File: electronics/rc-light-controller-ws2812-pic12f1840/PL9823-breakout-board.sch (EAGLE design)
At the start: 7 parts

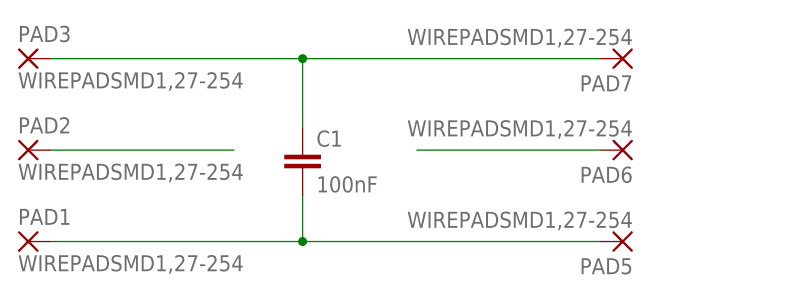
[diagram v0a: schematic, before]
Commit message: Finish breakout board, tweak light controller board
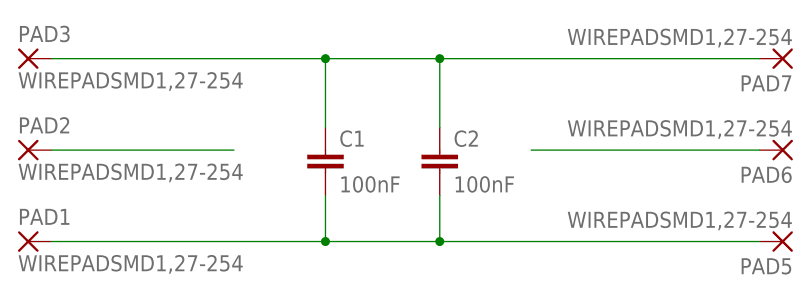
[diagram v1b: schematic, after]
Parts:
- added C2: 100nF, rcl:C-EUC0805K
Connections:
- net +: now also C2.1
- net -: now also C2.2
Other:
- moved on the sheet: C1, PAD5, PAD6, PAD7
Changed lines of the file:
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@@
 <part name="PAD7" library="wirepad" deviceset="WIREPAD" device="SMD1,27-254" value="WIREPADSMD1,27-254"/>
 <part name="C1" library="rcl" deviceset="C-EU" device="C0805K" value="100nF"/>
+<part name="C2" library="rcl" deviceset="C-EU" device="C0805K" value="100nF"/>
 </parts>
 <sheets>
@@
 <instance part="PAD2" gate="G$1" x="5.08" y="40.64"/>
 <instance part="PAD3" gate="G$1" x="5.08" y="50.8"/>
-<instance part="PAD5" gate="G$1" x="71.12" y="30.48" rot="R180"/>
-<instance part="PAD6" gate="G$1" x="71.12" y="40.64" rot="R180"/>
-<instance part="PAD7" gate="G$1" x="71.12" y="50.8" rot="R180"/>
-<instance part="C1" gate="G$1" x="35.56" y="40.64"/>
+<instance part="PAD5" gate="G$1" x="88.9" y="30.48" rot="R180"/>
+<instance part="PAD6" gate="G$1" x="88.9" y="40.64" rot="R180"/>
+<instance part="PAD7" gate="G$1" x="88.9" y="50.8" rot="R180"/>
+<instance part="C1" gate="G$1" x="38.1" y="40.64"/>
+<instance part="C2" gate="G$1" x="50.8" y="40.64"/>
 </instances>
 <busses>
@@
 <pinref part="PAD3" gate="G$1" pin="P"/>
 <pinref part="PAD7" gate="G$1" pin="P"/>
-<wire x1="7.62" y1="50.8" x2="35.56" y2="50.8" width="0.1524" layer="91"/>
+<wire x1="7.62" y1="50.8" x2="38.1" y2="50.8" width="0.1524" layer="91"/>
 <pinref part="C1" gate="G$1" pin="1"/>
-<wire x1="35.56" y1="50.8" x2="68.58" y2="50.8" width="0.1524" layer="91"/>
-<wire x1="35.56" y1="43.18" x2="35.56" y2="50.8" width="0.1524" layer="91"/>
-<junction x="35.56" y="50.8"/>
+<wire x1="38.1" y1="50.8" x2="50.8" y2="50.8" width="0.1524" layer="91"/>
+<wire x1="50.8" y1="50.8" x2="86.36" y2="50.8" width="0.1524" layer="91"/>
+<wire x1="38.1" y1="43.18" x2="38.1" y2="50.8" width="0.1524" layer="91"/>
+<junction x="38.1" y="50.8"/>
+<pinref part="C2" gate="G$1" pin="1"/>
+<wire x1="50.8" y1="43.18" x2="50.8" y2="50.8" width="0.1524" layer="91"/>
+<junction x="50.8" y="50.8"/>
 </segment>
 </net>
@@
 <pinref part="PAD1" gate="G$1" pin="P"/>
 <pinref part="PAD5" gate="G$1" pin="P"/>
-<wire x1="7.62" y1="30.48" x2="35.56" y2="30.48" width="0.1524" layer="91"/>
+<wire x1="7.62" y1="30.48" x2="38.1" y2="30.48" width="0.1524" layer="91"/>
 <pinref part="C1" gate="G$1" pin="2"/>
-<wire x1="35.56" y1="30.48" x2="68.58" y2="30.48" width="0.1524" layer="91"/>
-<wire x1="35.56" y1="35.56" x2="35.56" y2="30.48" width="0.1524" layer="91"/>
-<junction x="35.56" y="30.48"/>
+<wire x1="38.1" y1="30.48" x2="50.8" y2="30.48" width="0.1524" layer="91"/>
+<wire x1="50.8" y1="30.48" x2="86.36" y2="30.48" width="0.1524" layer="91"/>
+<wire x1="38.1" y1="35.56" x2="38.1" y2="30.48" width="0.1524" layer="91"/>
+<junction x="38.1" y="30.48"/>
+<pinref part="C2" gate="G$1" pin="2"/>
+<wire x1="50.8" y1="35.56" x2="50.8" y2="30.48" width="0.1524" layer="91"/>
+<junction x="50.8" y="30.48"/>
 </segment>
 </net>
@@
 <segment>
 <pinref part="PAD6" gate="G$1" pin="P"/>
-<wire x1="68.58" y1="40.64" x2="48.26" y2="40.64" width="0.1524" layer="91"/>
+<wire x1="86.36" y1="40.64" x2="60.96" y2="40.64" width="0.1524" layer="91"/>
 </segment>
 </net>
